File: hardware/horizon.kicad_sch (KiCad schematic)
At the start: 35 parts, among them J1 Conn_01x02_Pin, J2 Conn_01x06_Pin, J3 USB_C_Receptacle_USB2.0_14P, J4 Conn_01x14_Pin, J6 Conn_01x02_Pin, SW1 SW_Push, U1 ESP32-S3, U2 NCP1529A, U3 W25Q128JVS, U4 BQ24074RGT, Y1 CDX-1293

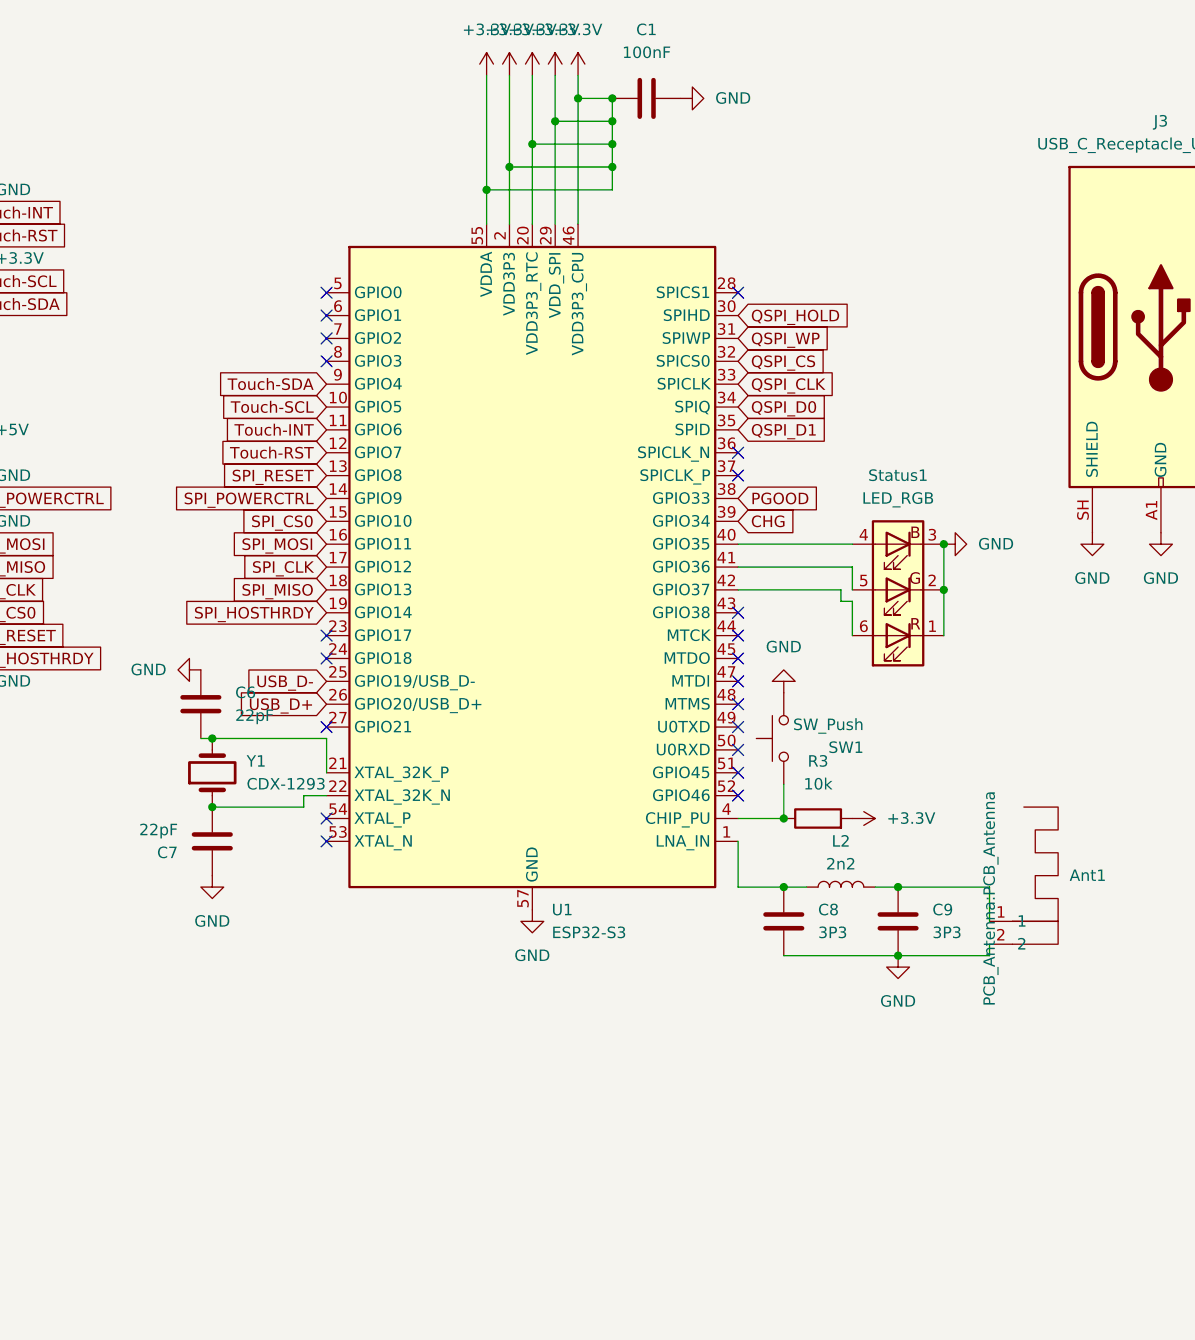
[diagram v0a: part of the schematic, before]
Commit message: Added haptic and sleep button
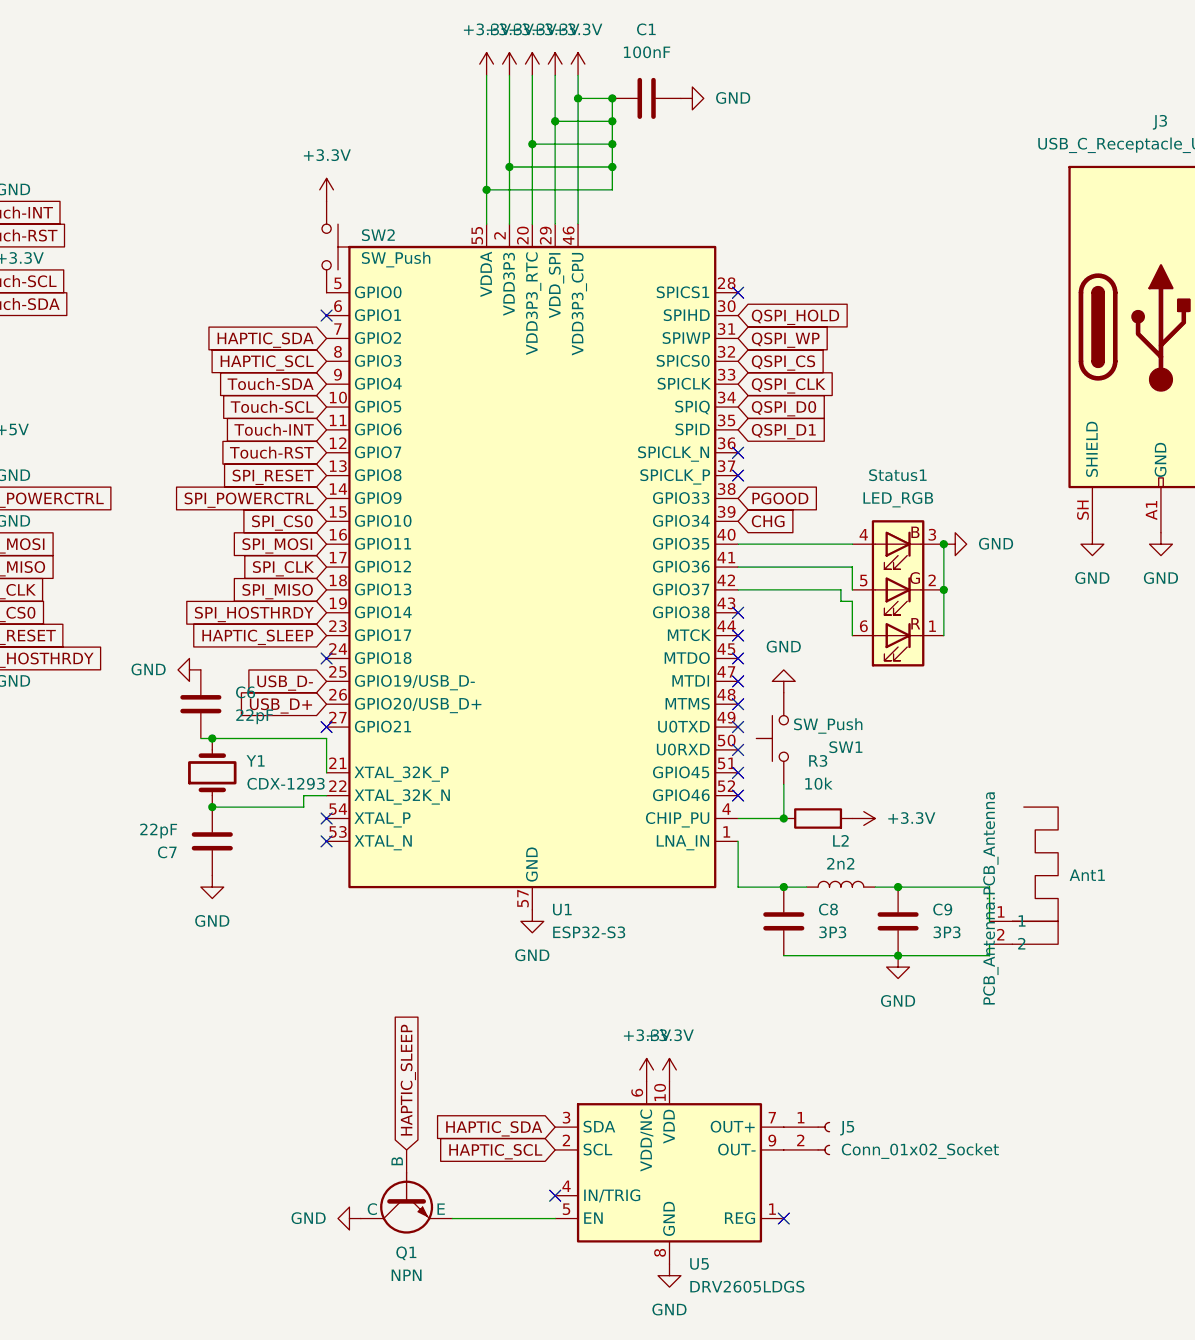
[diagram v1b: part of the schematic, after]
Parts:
- added J5: Conn_01x02_Socket, Solder Pads:2x solder pads, symbol Connector:Conn_01x02_Socket
- added Q1: NPN, Package_TO_SOT_THT:TO-92L, symbol Simulation_SPICE:NPN
- added SW2: SW_Push, Button_Switch_THT:SW_Push_1P2T_Vertical_E-Switch_800UDP8P1A1M6, symbol Switch:SW_Push
- added U5: DRV2605LDGS, Package_SO:TSSOP-10_3x3mm_P0.5mm, symbol Driver:DRV2605LDGS
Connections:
- net +3.3V: now also SW2.1, U5.10 (VDD), U5.6 (VDD/NC)
- net GND: now also Q1.1 (C), U5.8 (GND)
- net HAPTIC_SLEEP: now reaches U1.23 (GPIO17)
- net HAPTIC_SLEEP: now also Q1.2 (B)
- net at U1.5 (GPIO0): now also SW2.2
- net HAPTIC_SDA: now reaches U1.7 (GPIO2)
- net HAPTIC_SDA: now also U5.3 (SDA)
- net HAPTIC_SCL: now reaches U1.8 (GPIO3)
- net HAPTIC_SCL: now also U5.2 (SCL)
- new net: Q1.3 (E), U5.5 (EN)
- new net: J5.1 (Pin_1), U5.7 (OUT+)
- new net: J5.2 (Pin_2), U5.9 (OUT-)
- no-connect marks 22 -> 20

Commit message: Redoing pcb and fixed schem
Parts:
- added C10, C15, C17, C18: 0.1uF, Capacitor_SMD:C_0201_0603Metric, symbol Device:C
- added C11, C12, C13, C16: 1uF, Capacitor_SMD:C_0201_0603Metric, symbol Device:C
- added C14: 10nF, Capacitor_SMD:C_0201_0603Metric, symbol Device:C
- added C19: TBD, Capacitor_SMD:C_0201_0603Metric, symbol Device:C
- added D2, D3: D_TVS, Diode_SMD:D_0402_1005Metric, symbol Device:D_TVS
- added L3: L, Inductor_SMD:L_Bourns_SDR0604, symbol Device:L
- added L4: TBD, Inductor_SMD:L_Bourns_SDR0604, symbol Device:L
- added U6: ESP-PSRAM64H, Package_SO:SOIC-8_5.3x5.3mm_P1.27mm, symbol Memory_Flash:W25Q128JVS
- C1: value 100nF -> 0.1uF; footprint Capacitor_SMD:C_0201_0603Metric -> Diode_SMD:D_0402_1005Metric
- C2: value 100nF -> 10uF
- C8, C9: value 3P3 -> TBD
- L2: value 2n2 -> TBD
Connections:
- net +3.3V: now also C10.1, C11.1, C12.1, C13.1, C14.1, C15.1, C16.1, C17.1, C18.1, D2.1 (A1), L3.1, U6.8 (VCC); no longer C1.1, U1.2 (VDD3P3), U1.3 (VDD3P3)
- net GND: now also C10.2, C11.2, C12.2, C13.2, C14.2, C15.2, C16.2, C17.2, C18.2, C19.2, D2.2 (A2), D3.2 (A2), U6.4 (GND)
- net QSPI_CLK: now also U6.6 (CLK)
- net QSPI_CS: now also U6.1 (~{CS})
- net QSPI_D0: now also U6.2 (DO/IO_{1})
- net QSPI_D1: now also U6.5 (DI/IO_{0})
- net QSPI_HOLD: now also U6.7 (~{HOLD}/~{RESET}/IO_{3})
- net QSPI_WP: now also U6.3 (~{WP}/IO_{2})
- net at C9.1, L2.2: now also C19.1, L4.1; no longer Ant1.1
- new net: C1.1, L3.2, U1.2 (VDD3P3), U1.3 (VDD3P3)
- new net: Ant1.1, D3.1 (A1), L4.2
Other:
- note added: "LNA_IN"
- note added: "RF_ANT"

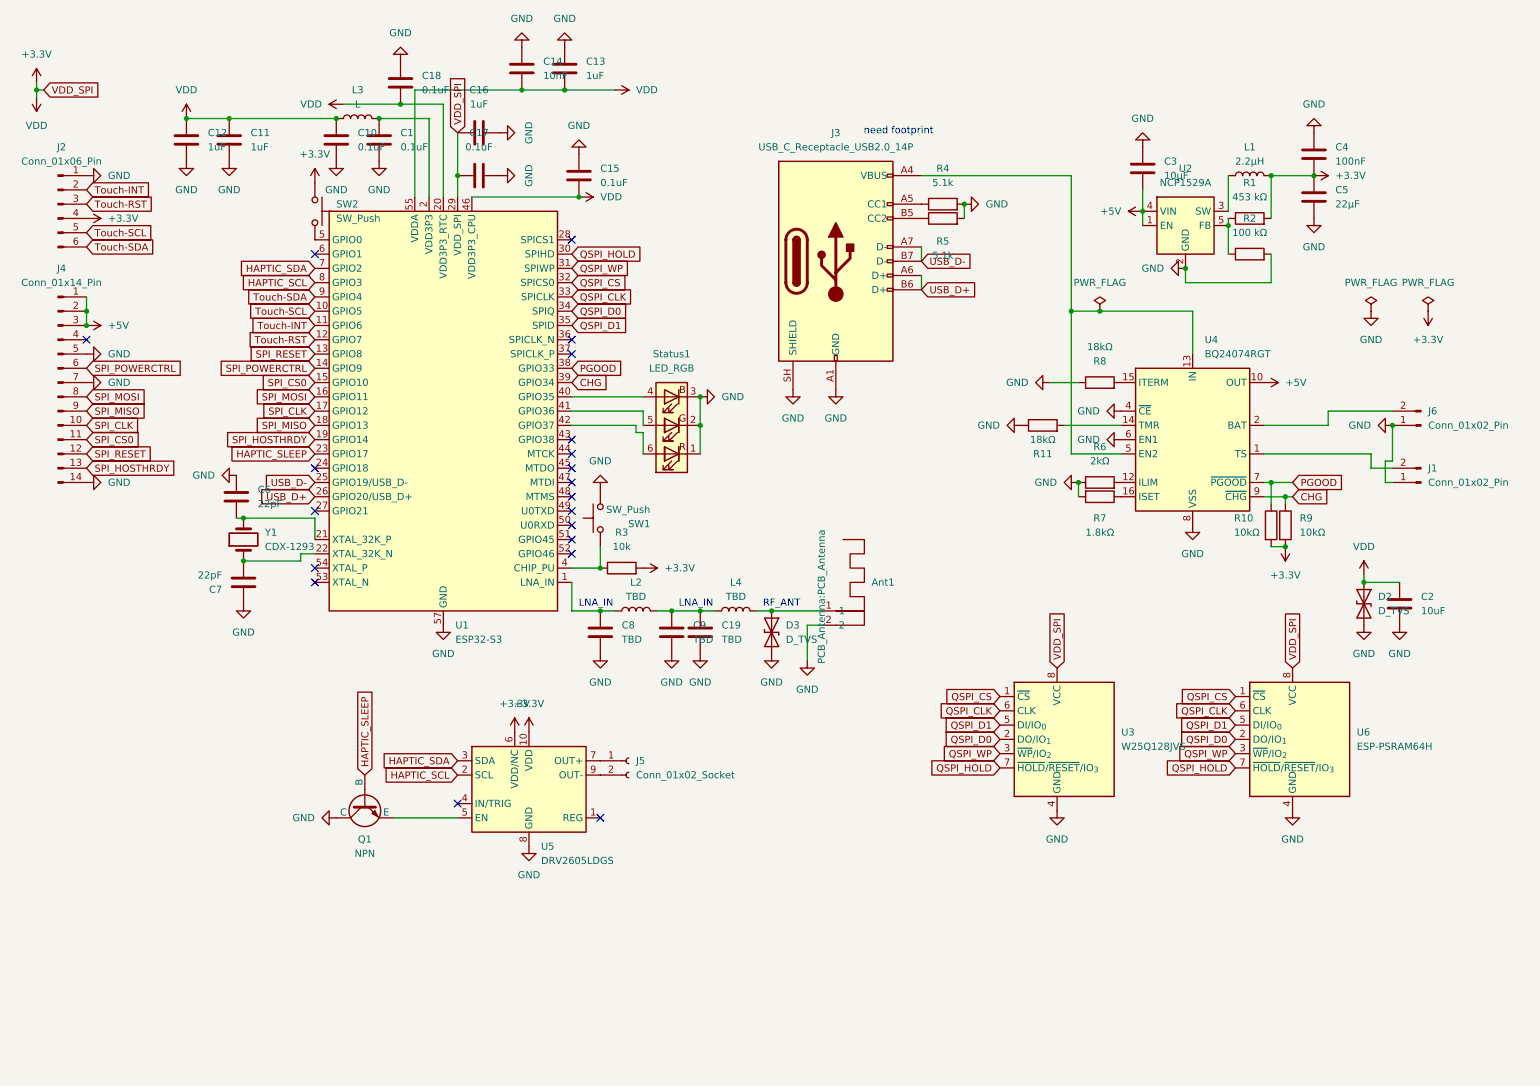
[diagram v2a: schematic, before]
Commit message: Adding SD card slot
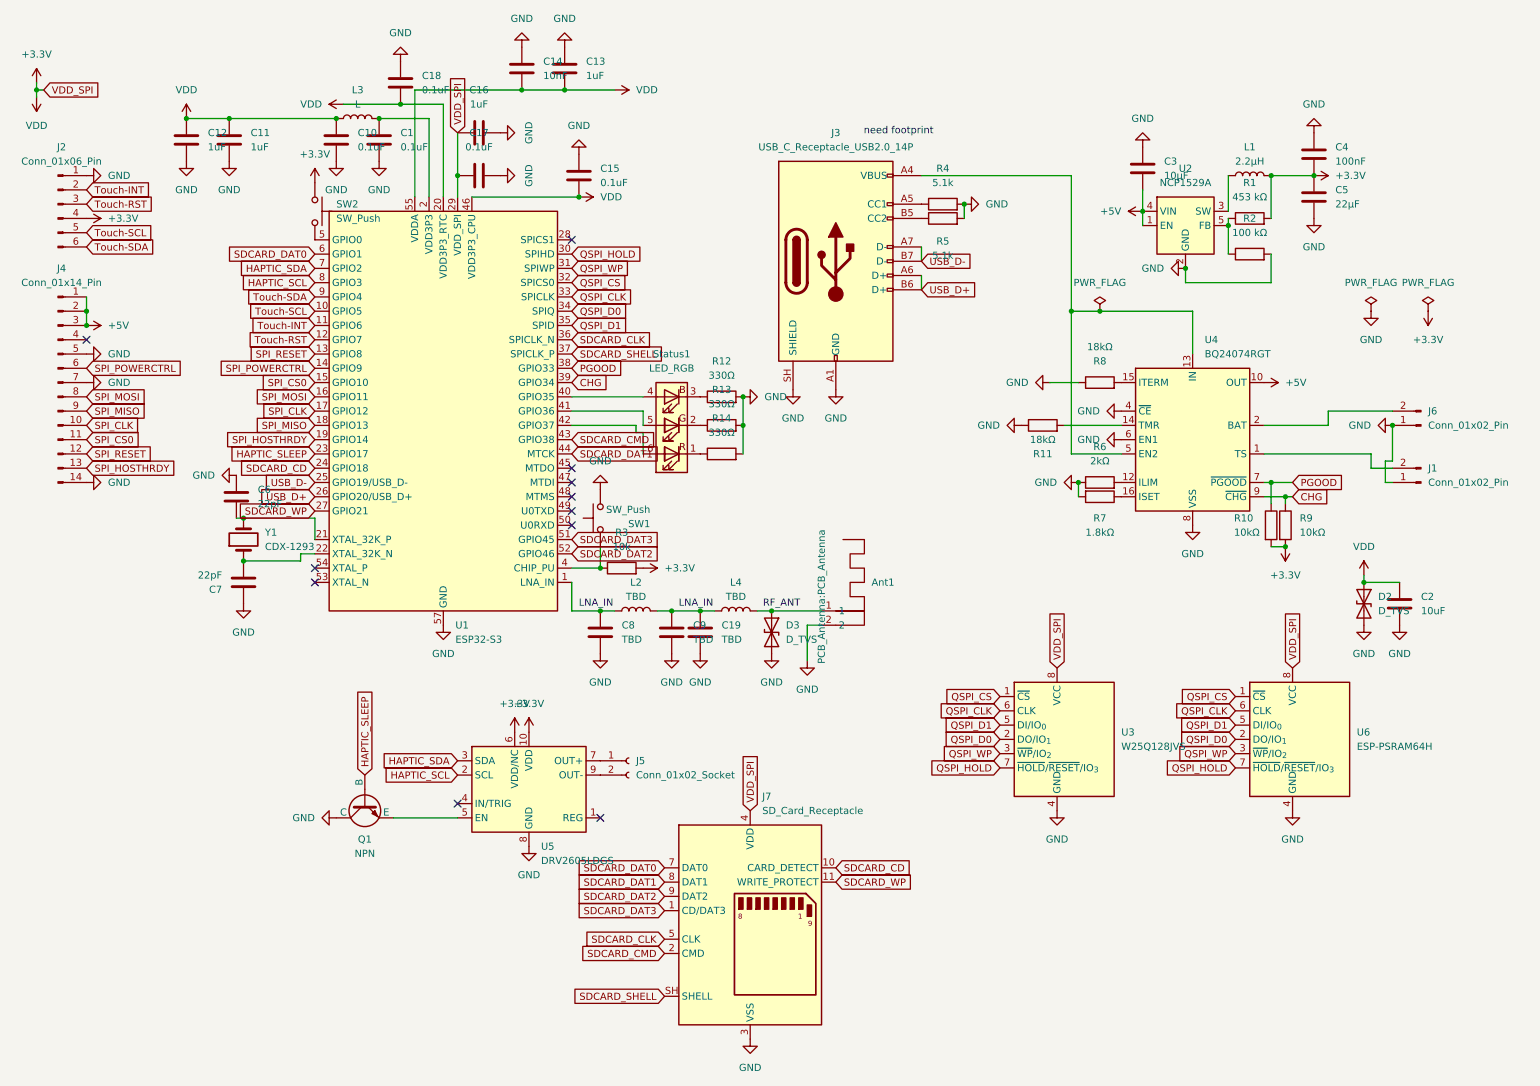
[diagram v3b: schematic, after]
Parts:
- added J7: SD_Card_Receptacle, Connector_Card:SD_TE_2041021, symbol Connector:SD_Card_Receptacle
- added R12, R13, R14: 330Ω, Resistor_SMD:R_0603_1608Metric, symbol Device:R
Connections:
- net +3.3V: now also J7.4 (VDD)
- net GND: now also J7.3 (VSS), J7.6 (VSS), R12.2, R13.2, R14.2; no longer Status1.1 (RK), Status1.2 (GK), Status1.3 (BK)
- net SDCARD_CD: now reaches U1.24 (GPIO18)
- net SDCARD_CD: now also J7.10 (CARD_DETECT)
- net SDCARD_WP: now reaches U1.27 (GPIO21)
- net SDCARD_WP: now also J7.11 (WRITE_PROTECT)
- net SDCARD_CLK: now reaches U1.36 (SPICLK_N)
- net SDCARD_CLK: now also J7.5 (CLK)
- net SDCARD_SHELL: now reaches U1.37 (SPICLK_P)
- net SDCARD_SHELL: now also J7.SH (SHELL)
- net SDCARD_CMD: now reaches U1.43 (GPIO38)
- net SDCARD_CMD: now also J7.2 (CMD)
- net SDCARD_DAT1: now reaches U1.44 (MTCK)
- net SDCARD_DAT1: now also J7.8 (DAT1)
- net SDCARD_DAT3: now reaches U1.51 (GPIO45)
- net SDCARD_DAT3: now also J7.1 (CD/DAT3)
- net SDCARD_DAT2: now reaches U1.52 (GPIO46)
- net SDCARD_DAT2: now also J7.9 (DAT2)
- net SDCARD_DAT0: now reaches U1.6 (GPIO1)
- net SDCARD_DAT0: now also J7.7 (DAT0)
- new net: R14.1, Status1.1 (RK)
- new net: R13.1, Status1.2 (GK)
- new net: R12.1, Status1.3 (BK)
- no-connect marks 20 -> 11
